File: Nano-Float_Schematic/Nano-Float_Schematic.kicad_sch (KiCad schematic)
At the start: 8 parts, among them M1 Motor_DC, SW1 SW_DIP_x01, U1 MS5837-xxBA

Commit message: updated float schematic
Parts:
- added C1: C_Small, symbol Device:C_Small
- added R2, R3: R, symbol Device:R
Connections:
- net 3V3: now also U1.2 (VDD), C1.2, R2.2, R3.2
- net GND: now also U1.1 (GND), C1.1
- net at U1.3 (SCL): now also R2.1
- net SDA: now reaches U1.4 (SDA)
- net SDA: now also R3.1
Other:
- moved on the sheet: U1
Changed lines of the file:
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@@
 (kicad_sch (version 20230121) (generator eeschema)
   (paper "A4")
+  (junction (at 87.63 57.15) (diameter 0) (color 0 0 0 0)
+  )
+  (junction (at 80.01 57.15) (diameter 0) (color 0 0 0 0)
+  )
+  (junction (at 80.01 78.74) (diameter 0) (color 0 0 0 0)
+  )
+  (junction (at 85.09 57.15) (diameter 0) (color 0 0 0 0)
+  )
   (junction (at 218.44 104.14) (diameter 0) (color 0 0 0 0)
   )
+  (wire (pts (xy 87.63 57.15) (xy 90.17 57.15))
+    (stroke (width 0) (type default))
+  )
+  (wire (pts (xy 80.01 57.15) (xy 85.09 57.15))
+    (stroke (width 0) (type default))
+  )
+  (wire (pts (xy 80.01 80.01) (xy 80.01 78.74))
+    (stroke (width 0) (type default))
+  )
   (wire (pts (xy 151.13 91.44) (xy 162.56 91.44))
     (stroke (width 0) (type default))
@@
     (stroke (width 0) (type default))
   )
+  (wire (pts (xy 83.82 80.01) (xy 80.01 80.01))
+    (stroke (width 0) (type default))
+  )
   (wire (pts (xy 114.3 118.11) (xy 114.3 127))
     (stroke (width 0) (type default))
@@
     (stroke (width 0) (type default))
   )
+  (wire (pts (xy 62.23 58.42) (xy 62.23 57.15))
+    (stroke (width 0) (type default))
+  )
   (wire (pts (xy 151.13 83.82) (xy 162.56 83.82))
     (stroke (width 0) (type default))
   )
+  (wire (pts (xy 85.09 57.15) (xy 87.63 57.15))
+    (stroke (width 0) (type default))
+  )
   (wire (pts (xy 177.8 83.82) (xy 186.69 83.82))
     (stroke (width 0) (type default))
@@
     (stroke (width 0) (type default))
   )
+  (wire (pts (xy 58.42 82.55) (xy 58.42 50.8))
+    (stroke (width 0) (type default))
+  )
   (wire (pts (xy 69.85 95.25) (xy 69.85 102.87))
     (stroke (width 0) (type default))
@@
     (stroke (width 0) (type default))
   )
+  (wire (pts (xy 91.44 82.55) (xy 58.42 82.55))
+    (stroke (width 0) (type default))
+  )
+  (wire (pts (xy 87.63 64.77) (xy 87.63 66.04))
+    (stroke (width 0) (type default))
+  )
+  (wire (pts (xy 58.42 50.8) (xy 81.28 50.8))
+    (stroke (width 0) (type default))
+  )
+  (wire (pts (xy 62.23 57.15) (xy 80.01 57.15))
+    (stroke (width 0) (type default))
+  )
   (wire (pts (xy 151.13 80.01) (xy 151.13 83.82))
     (stroke (width 0) (type default))
@@
     (stroke (width 0) (type default))
   )
+  (wire (pts (xy 81.28 49.53) (xy 85.09 49.53))
+    (stroke (width 0) (type default))
+  )
+  (wire (pts (xy 91.44 68.58) (xy 91.44 82.55))
+    (stroke (width 0) (type default))
+  )
   (wire (pts (xy 170.18 69.85) (xy 170.18 80.01))
     (stroke (width 0) (type default))
@@
     (stroke (width 0) (type default))
   )
+  (wire (pts (xy 62.23 78.74) (xy 80.01 78.74))
+    (stroke (width 0) (type default))
+  )
   (wire (pts (xy 127 111.76) (xy 134.62 111.76))
     (stroke (width 0) (type default))
@@
     (stroke (width 0) (type default))
   )
+  (wire (pts (xy 87.63 68.58) (xy 91.44 68.58))
+    (stroke (width 0) (type default))
+  )
+  (wire (pts (xy 81.28 50.8) (xy 81.28 49.53))
+    (stroke (width 0) (type default))
+  )
+  (wire (pts (xy 80.01 58.42) (xy 80.01 57.15))
+    (stroke (width 0) (type default))
+  )
+  (wire (pts (xy 62.23 63.5) (xy 62.23 78.74))
+    (stroke (width 0) (type default))
+  )
   (wire (pts (xy 218.44 104.14) (xy 220.98 104.14))
     (stroke (width 0) (type default))
@@
     (stroke (width 0) (type default))
   )
-  (rectangle (start 53.34 46.99) (end 93.98 78.74)
+  (rectangle (start 53.34 46.99) (end 97.79 82.55)
     (stroke (width 0) (type default))
     (fill (type none))
@@
     (effects (font (size 1.27 1.27)) (justify left bottom))
   )
-  (text "pressure sensor\n" (at 68.58 50.8 0)
+  (text "pressure sensor\n" (at 54.61 49.53 0)
     (effects (font (size 1.27 1.27)) (justify left bottom))
   )
@@
     )
   )
+  (global_label "SDA" (shape input) (at 91.44 68.58 0) (fields_autoplaced)
+    (effects (font (size 1.27 1.27)) (justify left))
+    (property "Intersheetrefs" "${INTERSHEET_REFS}" (at 97.9933 68.58 0)
+      (effects (font (size 1.27 1.27)) (justify left) hide)
+    )
+  )
+  (global_label "GND" (shape input) (at 83.82 80.01 0) (fields_autoplaced)
+    (effects (font (size 1.27 1.27)) (justify left))
+    (property "Intersheetrefs" "${INTERSHEET_REFS}" (at 90.6757 80.01 0)
+      (effects (font (size 1.27 1.27)) (justify left) hide)
+    )
+  )
   (global_label "OUT4" (shape output) (at 186.69 91.44 0) (fields_autoplaced)
     (effects (font (size 1.27 1.27)) (justify left))
@@
     (effects (font (size 1.27 1.27)) (justify left))
     (property "Intersheetrefs" "${INTERSHEET_REFS}" (at 194.5133 83.82 0)
+      (effects (font (size 1.27 1.27)) (justify left) hide)
+    )
+  )
+  (global_label "3V3" (shape input) (at 90.17 57.15 0) (fields_autoplaced)
+    (effects (font (size 1.27 1.27)) (justify left))
+    (property "Intersheetrefs" "${INTERSHEET_REFS}" (at 96.6628 57.15 0)
       (effects (font (size 1.27 1.27)) (justify left) hide)
     )
@@
     )
   )
-  (symbol (lib_id "Sensor_Pressure:MS5837-xxBA") (at 76.2 64.77 0) (unit 1)
-    (in_bom yes) (on_board yes) (dnp no) (fields_autoplaced)
-    (property "Reference" "U1" (at 69.85 63.5 0)
+  (symbol (lib_id "Device:R") (at 85.09 53.34 0) (unit 1)
+    (in_bom yes) (on_board yes) (dnp no)
+    (property "Reference" "R3" (at 87.63 52.07 0)
+      (effects (font (size 1.27 1.27)) (justify left))
+    )
+    (property "Value" "R" (at 87.63 54.61 0)
+      (effects (font (size 1.27 1.27)) (justify left))
+    )
+    (property "Footprint" "" (at 83.312 53.34 90)
+      (effects (font (size 1.27 1.27)) hide)
+    )
+    (property "Datasheet" "~" (at 85.09 53.34 0)
+      (effects (font (size 1.27 1.27)) hide)
+    )
+    (pin "2")
+    (pin "1")
+    (instances
+      (project "Nano-Float_Schematic"
+        (path "/f729cb88-08f1-4e9e-8512-18a9fe0c9c6f"
+          (reference "R3") (unit 1)
+        )
+      )
+    )
+  )
+  (symbol (lib_id "Sensor_Pressure:MS5837-xxBA") (at 80.01 68.58 0) (unit 1)
+    (in_bom yes) (on_board yes) (dnp no) (fields_autoplaced)
+    (property "Reference" "U1" (at 73.66 67.31 0)
       (effects (font (size 1.27 1.27)) (justify right))
     )
-    (property "Value" "MS5837-xxBA" (at 69.85 66.04 0)
+    (property "Value" "MS5837-xxBA" (at 73.66 69.85 0)
       (effects (font (size 1.27 1.27)) (justify right))
     )
-    (property "Footprint" "Sensor_Pressure:TE_MS5837-xxBA" (at 76.2 64.77 0)
-      (effects (font (size 1.27 1.27)) hide)
-    )
-    (property "Datasheet" "https://www.te.com/commerce/DocumentDelivery/DDEController?Action=showdoc&DocId=Data+Sheet%7FMS5837-30BA%7FB1%7Fpdf%7FEnglish%7FENG_DS_MS5837-30BA_B1.pdf%7FCAT-BLPS0017" (at 76.2 67.31 0)
+    (property "Footprint" "Sensor_Pressure:TE_MS5837-xxBA" (at 80.01 68.58 0)
+      (effects (font (size 1.27 1.27)) hide)
+    )
+    (property "Datasheet" "https://www.te.com/commerce/DocumentDelivery/DDEController?Action=showdoc&DocId=Data+Sheet%7FMS5837-30BA%7FB1%7Fpdf%7FEnglish%7FENG_DS_MS5837-30BA_B1.pdf%7FCAT-BLPS0017" (at 80.01 71.12 0)
       (effects (font (size 1.27 1.27)) hide)
     )
@@
         )
       )
+    )
+  )
+  (symbol (lib_id "Device:C_Small") (at 62.23 60.96 180) (unit 1)
+    (in_bom yes) (on_board yes) (dnp no) (fields_autoplaced)
+    (property "Reference" "C1" (at 64.77 59.6836 0)
+      (effects (font (size 1.27 1.27)) (justify right))
+    )
+    (property "Value" "C_Small" (at 64.77 62.2236 0)
+      (effects (font (size 1.27 1.27)) (justify right))
+    )
+    (property "Footprint" "" (at 62.23 60.96 0)
+      (effects (font (size 1.27 1.27)) hide)
+    )
+    (property "Datasheet" "~" (at 62.23 60.96 0)
+      (effects (font (size 1.27 1.27)) hide)
+    )
+    (pin "2")
+    (pin "1")
+    (instances
+      (project "Nano-Float_Schematic"
+        (path "/f729cb88-08f1-4e9e-8512-18a9fe0c9c6f"
+          (reference "C1") (unit 1)
+        )
+      )
+    )
+  )
+  (symbol (lib_id "Device:R") (at 87.63 60.96 180) (unit 1)
+    (in_bom yes) (on_board yes) (dnp no) (fields_autoplaced)
+    (property "Reference" "R2" (at 90.17 59.69 0)
+      (effects (font (size 1.27 1.27)) (justify right))
+    )
+    (property "Value" "R" (at 90.17 62.23 0)
+      (effects (font (size 1.27 1.27)) (justify right))
+    )
+    (property "Footprint" "" (at 89.408 60.96 90)
+      (effects (font (size 1.27 1.27)) hide)
+    )
+    (property "Datasheet" "~" (at 87.63 60.96 0)
+      (effects (font (size 1.27 1.27)) hide)
+    )
+    (pin "2")
+    (pin "1")
+    (instances
+      (project "Nano-Float_Schematic"
+        (path "/f729cb88-08f1-4e9e-8512-18a9fe0c9c6f"
+          (reference "R2") (unit 1)
+        )
+      )

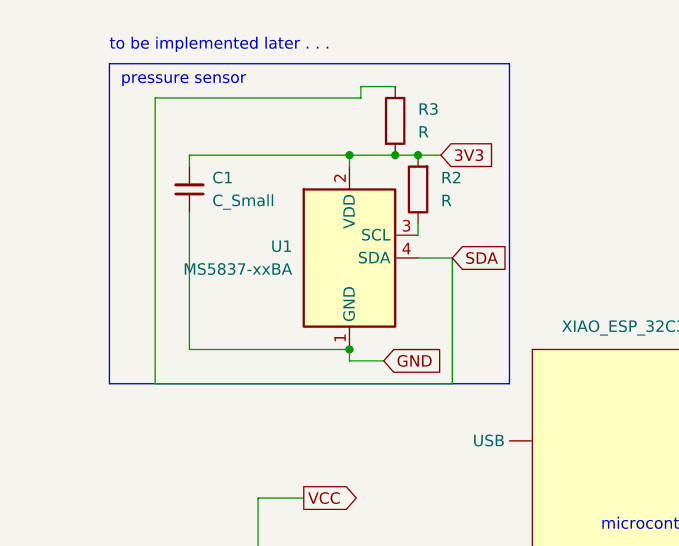
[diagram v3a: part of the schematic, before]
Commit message: Update Nano-Float_Schematic.kicad_sch
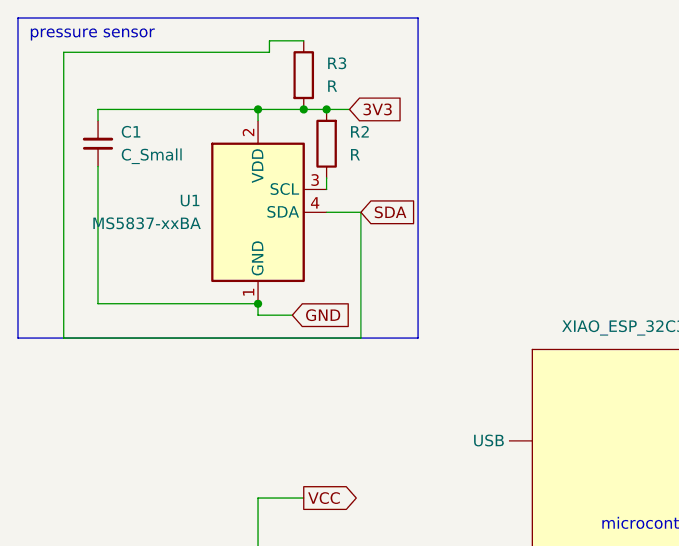
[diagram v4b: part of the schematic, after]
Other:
- note removed: "to be implemented later . . ."
- moved on the sheet: C1, R2, R3, U1
